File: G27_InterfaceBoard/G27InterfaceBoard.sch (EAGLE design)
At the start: 32 parts, among them IC1 LMV321M5, IC2 74HC126D, J1 Pedal, J2 Shifter, U1 LMV324

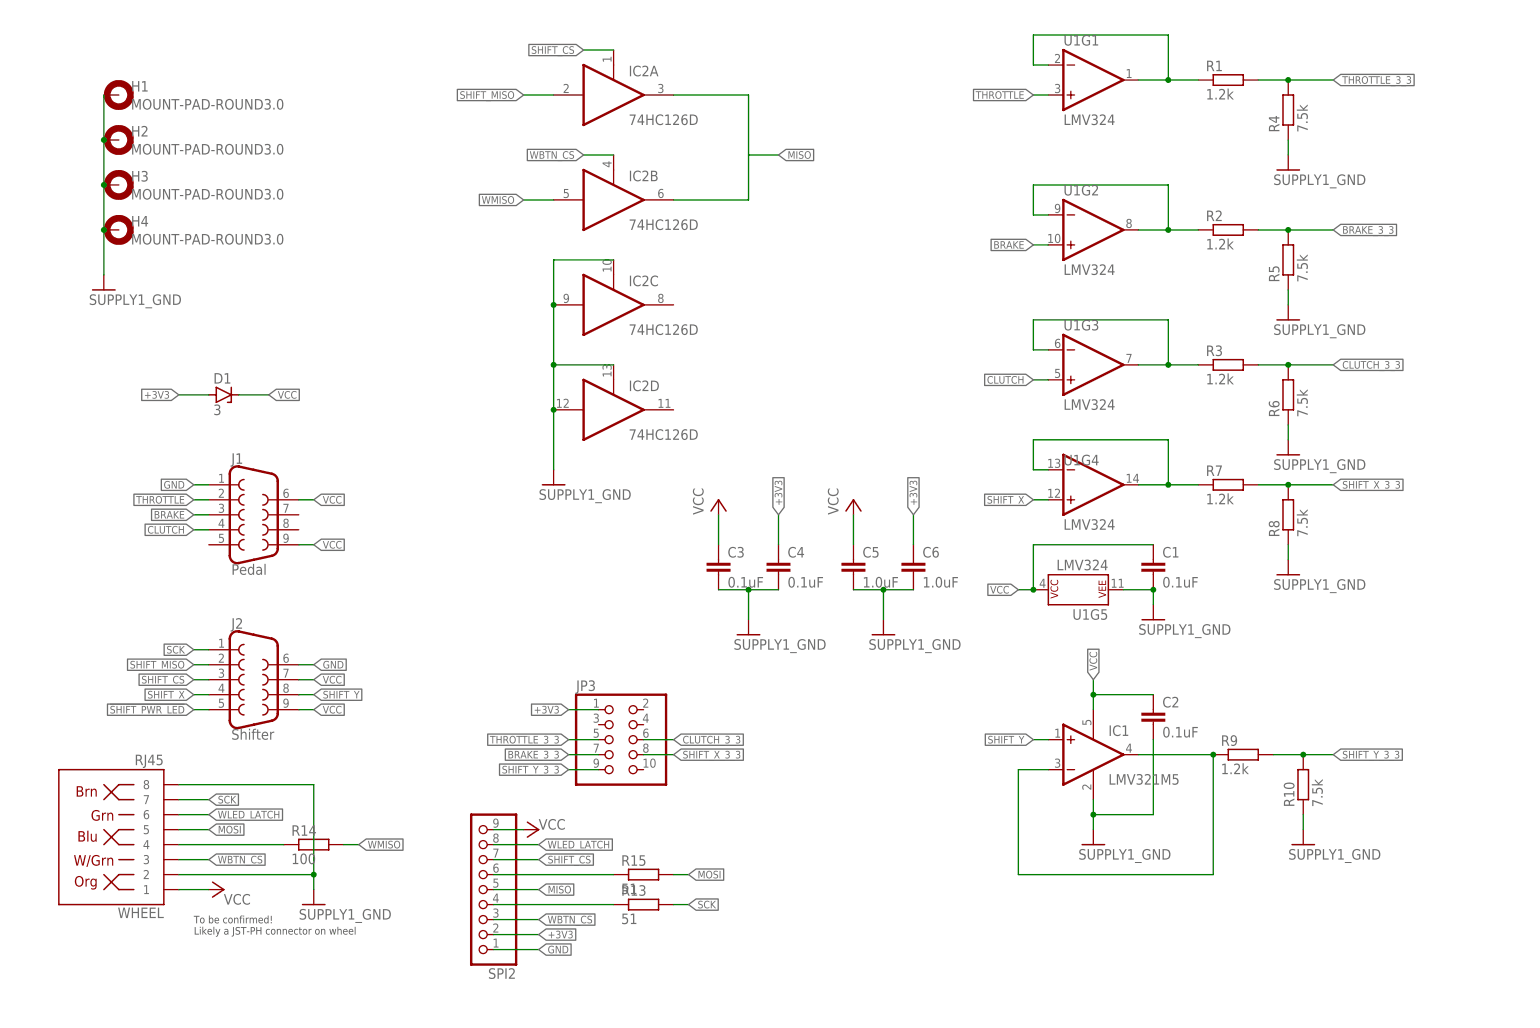
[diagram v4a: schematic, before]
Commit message: Closer on G27 Interface v1.1:
Use buffer to boost 3.3V signals from STM32 to 5V logic to buy
better noise margin.
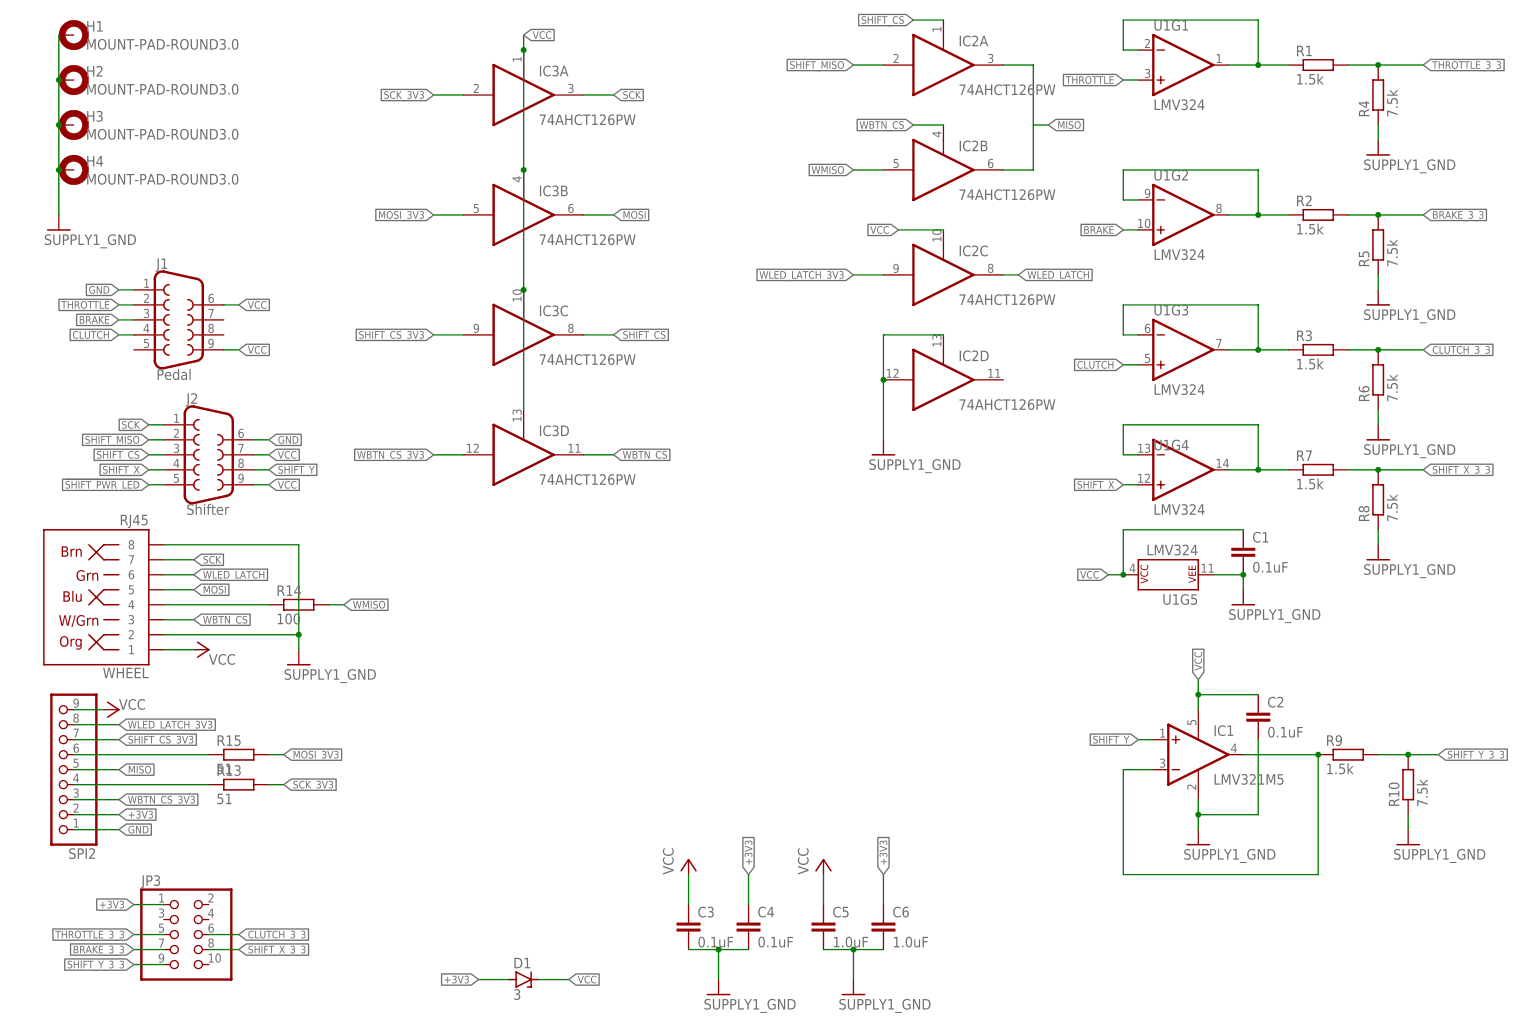
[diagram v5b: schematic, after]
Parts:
- added IC3: 74AHCT126PW, 74xx-eu:74AHCT126PW
- IC2: value 74HC126D -> 74AHCT126PW; device 74xx-eu:74HC126D -> 74xx-eu:74AHCT126PW
- R1, R2, R3, R7, R9: value 1.2k -> 1.5k
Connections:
- new net MOSI_3V3: IC3B.I, R15.2
- new net SCK_3V3: IC3A.I, R13.2
- new net SHIFT_CS_3V3: IC3C.I, SPI2.7
- new net WBTN_CS_3V3: IC3D.I, SPI2.3
- new net WLED_LATCH_3V3: IC2C.I, SPI2.8
- net GND: no longer IC2C.I, IC2C.OE
- net MOSI: now also IC3B.O; no longer R15.2
- net SCK: now also IC3A.O; no longer R13.2
- net SHIFT_CS: now also IC3C.O; no longer SPI2.7
- net VCC: now also IC2C.OE, IC3A.OE, IC3B.OE, IC3C.OE, IC3D.OE
- net WBTN_CS: now also IC3D.O; no longer SPI2.3
- net WLED_LATCH: now also IC2C.O; no longer SPI2.8
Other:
- note removed: "To be confirmed! Likely a JST-PH connector on wheel"
- moved on the sheet: C1, C2, C3, C4, C5, C6, D1, H1, H2, H3, H4, IC1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

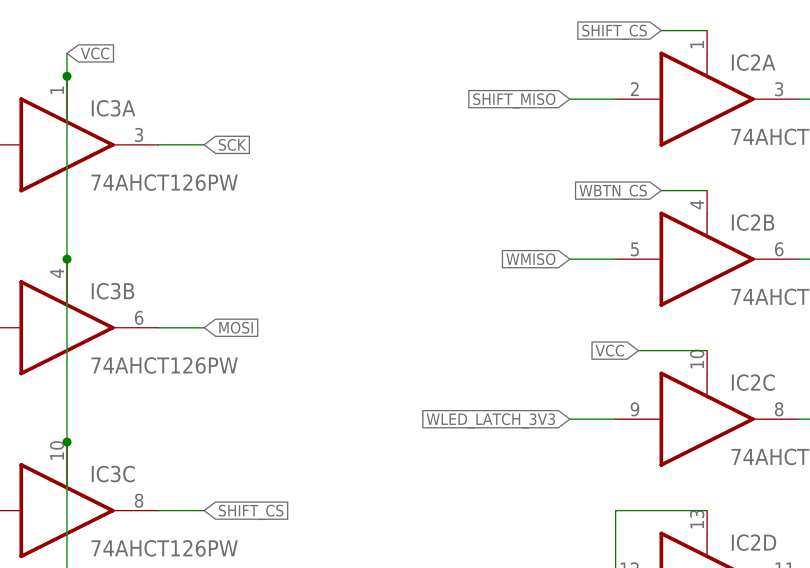
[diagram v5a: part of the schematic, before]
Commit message: Add additional filter caps.
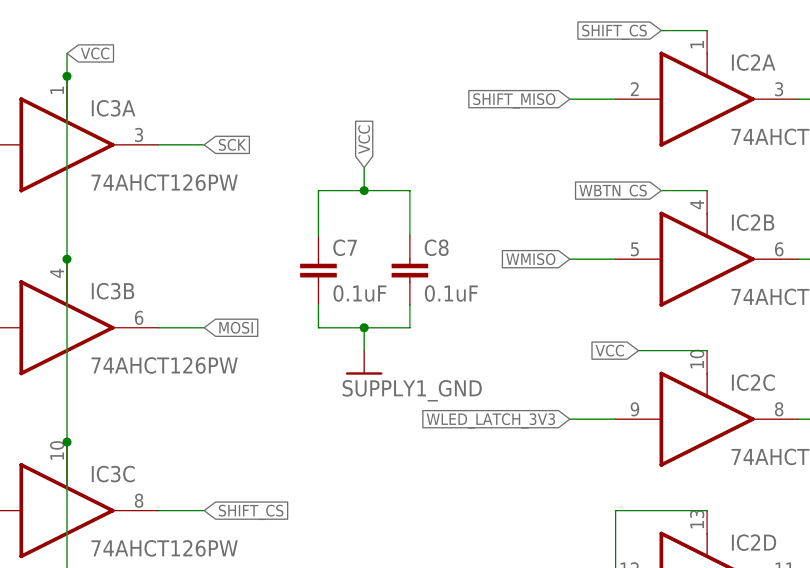
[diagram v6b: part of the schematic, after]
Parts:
- added C7, C8: 0.1uF, resistor:C-EUC0603
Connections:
- net GND: now also C7.2, C8.2
- net VCC: now also C7.1, C8.1
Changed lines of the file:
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@@
 <part name="R15" library="resistor" library_urn="urn:adsk.eagle:library:348" deviceset="R-EU_" device="R0603" package3d_urn="urn:adsk.eagle:package:23555/3" value="51"/>
 <part name="IC3" library="74xx-eu" deviceset="74*126" device="PW" package3d_urn="urn:adsk.eagle:package:2019/3" technology="AHCT"/>
+<part name="C7" library="resistor" library_urn="urn:adsk.eagle:library:348" deviceset="C-EU" device="C0603" package3d_urn="urn:adsk.eagle:package:23616/2" value="0.1uF"/>
+<part name="C8" library="resistor" library_urn="urn:adsk.eagle:library:348" deviceset="C-EU" device="C0603" package3d_urn="urn:adsk.eagle:package:23616/2" value="0.1uF"/>
+<part name="GND13" library="stm_board_f407" deviceset="SUPPLY1_GND" device=""/>
 </parts>
 <sheets>
@@
 <attribute name="NAME" x="88.9" y="102.235" size="1.778" layer="95"/>
 <attribute name="VALUE" x="88.9" y="93.98" size="1.778" layer="96"/>
+</instance>
+<instance part="C7" gate="G$1" x="114.3" y="147.32" smashed="yes">
+<attribute name="NAME" x="115.824" y="147.701" size="1.778" layer="95"/>
+<attribute name="VALUE" x="115.824" y="142.621" size="1.778" layer="96"/>
+</instance>
+<instance part="C8" gate="G$1" x="124.46" y="147.32" smashed="yes">
+<attribute name="NAME" x="125.984" y="147.701" size="1.778" layer="95"/>
+<attribute name="VALUE" x="125.984" y="142.621" size="1.778" layer="96"/>
+</instance>
+<instance part="GND13" gate="1" x="119.38" y="134.62" smashed="yes">
+<attribute name="VALUE" x="116.84" y="132.08" size="1.778" layer="96"/>
 </instance>
 </instances>
@@
 <label x="17.78" y="35.56" size="1.27" layer="95" xref="yes"/>
 </segment>
+<segment>
+<pinref part="C7" gate="G$1" pin="2"/>
+<wire x1="114.3" y1="142.24" x2="114.3" y2="139.7" width="0.1524" layer="91"/>
+<pinref part="C8" gate="G$1" pin="2"/>
+<wire x1="114.3" y1="139.7" x2="119.38" y2="139.7" width="0.1524" layer="91"/>
+<wire x1="119.38" y1="139.7" x2="124.46" y2="139.7" width="0.1524" layer="91"/>
+<wire x1="124.46" y1="139.7" x2="124.46" y2="142.24" width="0.1524" layer="91"/>
+<junction x="119.38" y="139.7"/>
+<pinref part="GND13" gate="1" pin="GND"/>
+<wire x1="119.38" y1="137.16" x2="119.38" y2="139.7" width="0.1524" layer="91"/>
+</segment>
 </net>
 <net name="SCK" class="0">
@@
 <junction x="86.36" y="127"/>
 </segment>
-</net>
+<segment>
+<pinref part="C7" gate="G$1" pin="1"/>
+<wire x1="114.3" y1="149.86" x2="114.3" y2="154.94" width="0.1524" layer="91"/>
+<pinref part="C8" gate="G$1" pin="1"/>
+<wire x1="114.3" y1="154.94" x2="119.38" y2="154.94" width="0.1524" layer="91"/>
+<wire x1="119.38" y1="154.94" x2="124.46" y2="154.94" width="0.1524" layer="91"/>
+<wire x1="124.46" y1="154.94" x2="124.46" y2="149.86" width="0.1524" layer="91"/>
+<junction x="119.38" y="154.94"/>
+<wire x1="119.38" y1="154.94" x2="119.38" y2="157.48" width="0.1524" layer="91"/>
+<label x="119.38" y="157.48" size="1.27" layer="95" rot="R90" xref="yes"/>
+</segment>
+</net>

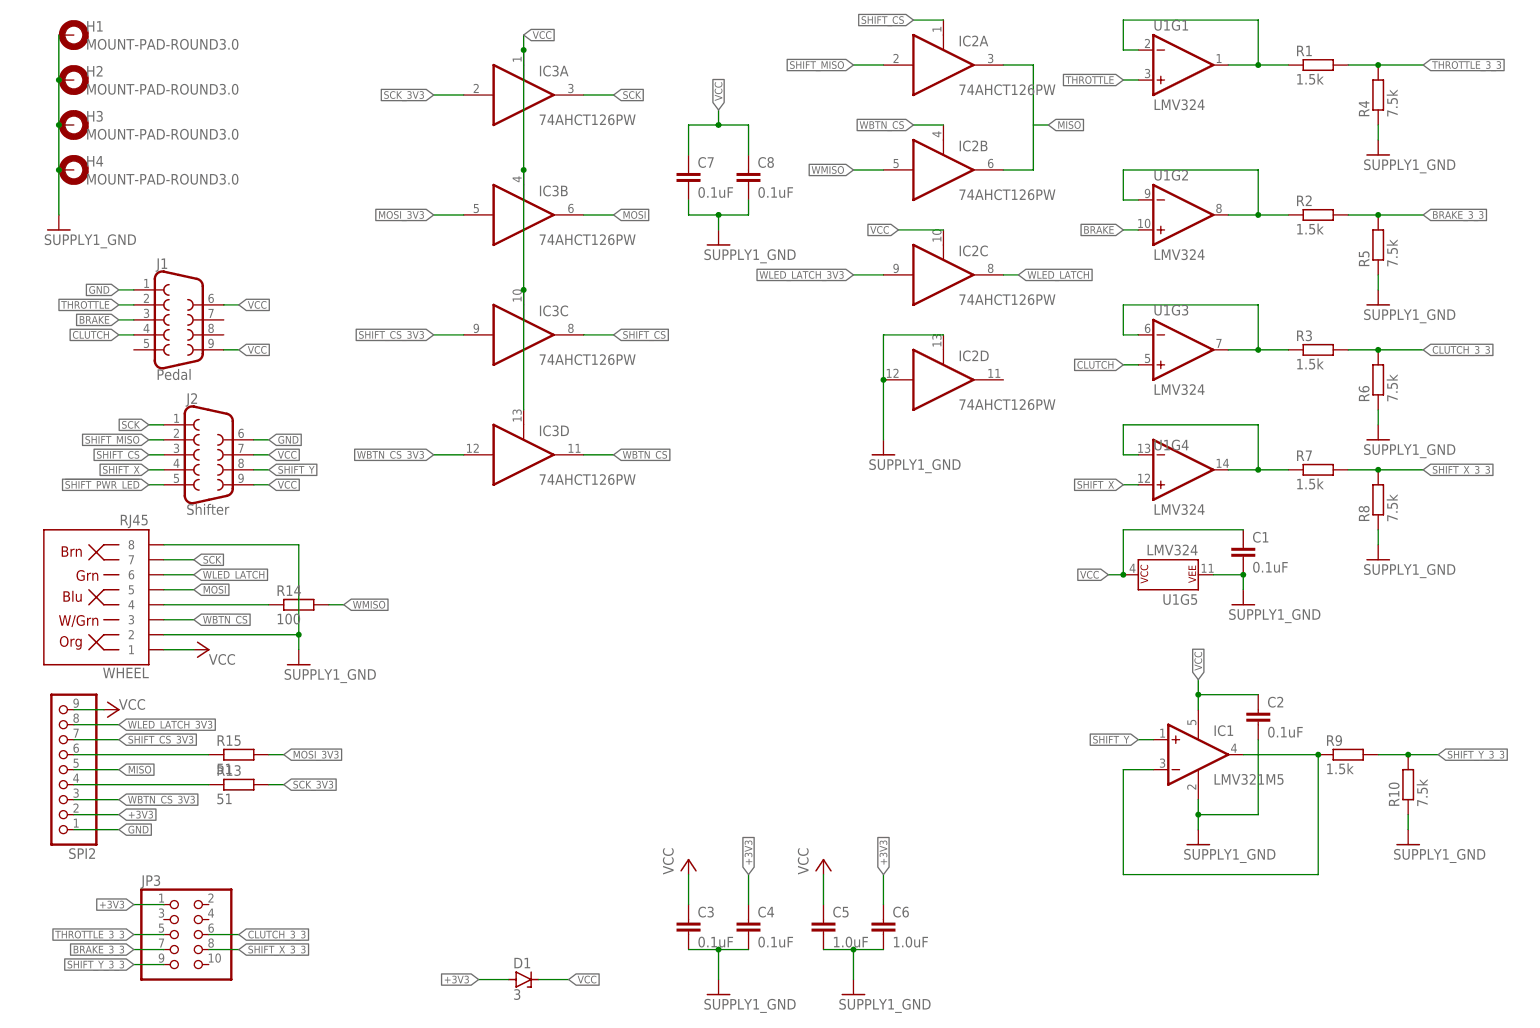
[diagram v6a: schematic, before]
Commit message: Add voltage clamps to signals that could go above 3.3V.
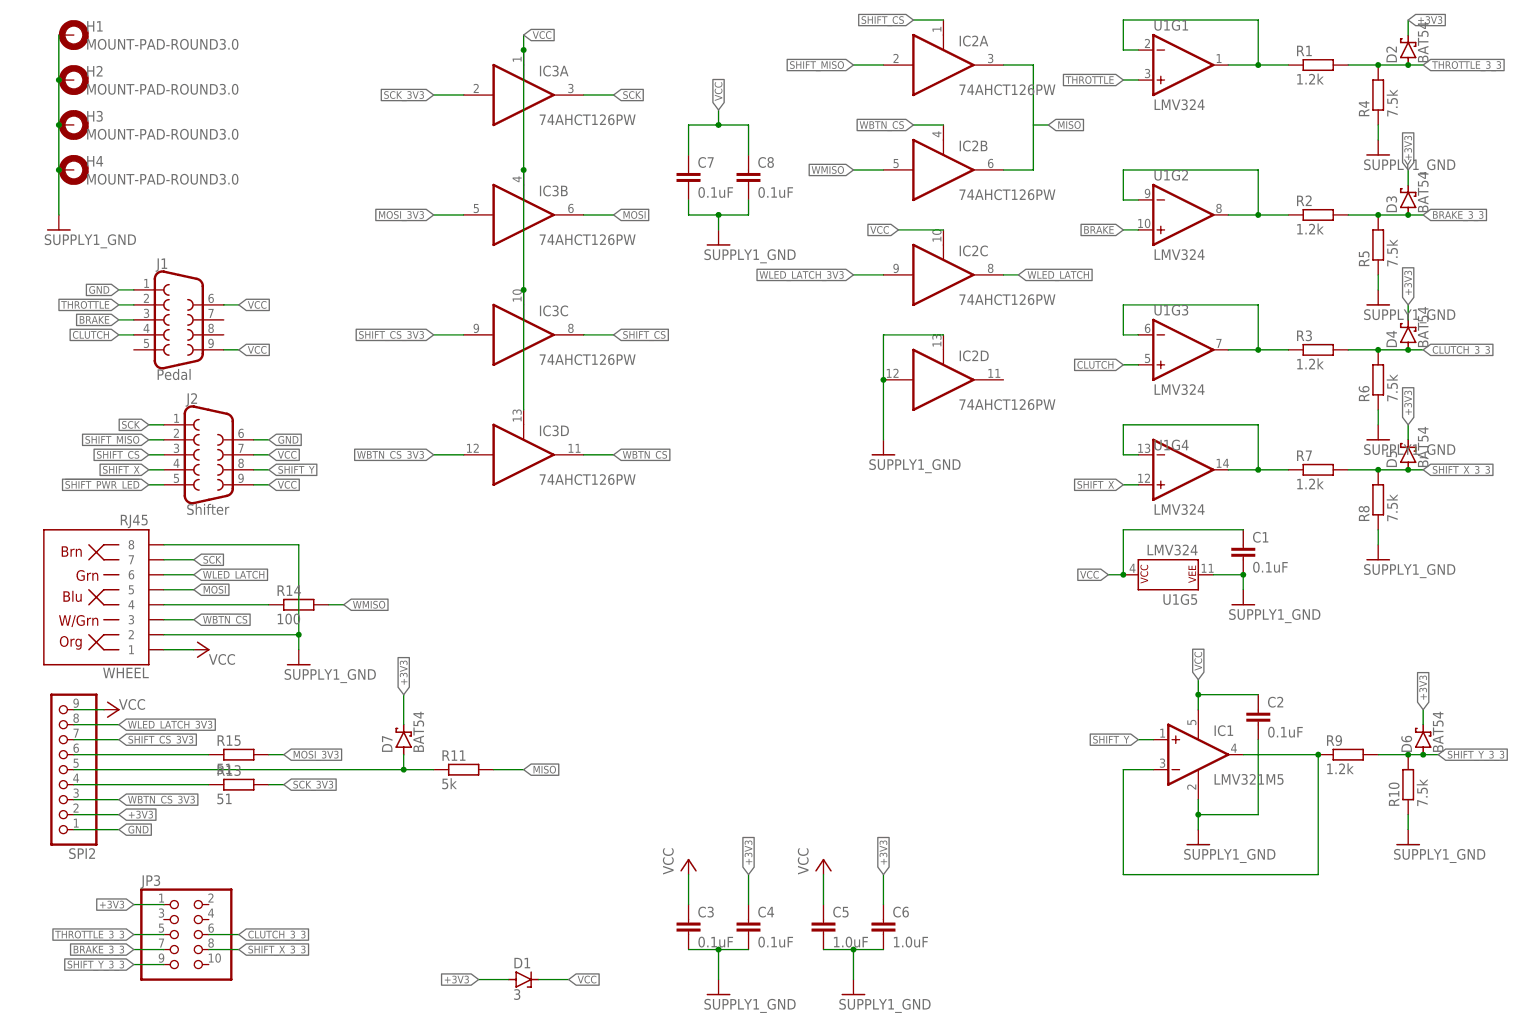
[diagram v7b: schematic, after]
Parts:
- added D2, D3, D4, D5, D6, D7: BAT54, diode:BAT54
- added R11: 5k, resistor:R-EU_R0603
- R1, R2, R3, R7, R9: value 1.5k -> 1.2k
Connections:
- new net N$4: D7.A, R11.1, SPI2.5
- net +3V3: now also D2.C, D3.C, D4.C, D5.C, D6.C, D7.C
- net BRAKE_3_3: now also D3.A
- net CLUTCH_3_3: now also D4.A
- net MISO: now also R11.2; no longer SPI2.5
- net SHIFT_X_3_3: now also D5.A
- net SHIFT_Y_3_3: now also D6.A
- net THROTTLE_3_3: now also D2.A

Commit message: Add better 5V, 3.3V, and GND connections.
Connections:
- net +3V3: now also JP3.2
- net GND: now also JP3.3, JP3.4
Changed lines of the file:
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@@
 <wire x1="119.38" y1="137.16" x2="119.38" y2="139.7" width="0.1524" layer="91"/>
+</segment>
+<segment>
+<pinref part="JP3" gate="A" pin="4"/>
+<wire x1="33.02" y1="20.32" x2="38.1" y2="20.32" width="0.1524" layer="91"/>
+<label x="38.1" y="20.32" size="1.27" layer="95" xref="yes"/>
+</segment>
+<segment>
+<pinref part="JP3" gate="A" pin="3"/>
+<wire x1="25.4" y1="20.32" x2="20.32" y2="20.32" width="0.1524" layer="91"/>
+<label x="20.32" y="20.32" size="1.27" layer="95" rot="R180" xref="yes"/>
 </segment>
 </net>
@@
 <label x="66.04" y="58.42" size="1.27" layer="95" rot="R90" xref="yes"/>
 </segment>
-</net>
+<segment>
+<pinref part="JP3" gate="A" pin="2"/>
+<wire x1="33.02" y1="22.86" x2="38.1" y2="22.86" width="0.1524" layer="91"/>
+<label x="38.1" y="22.86" size="1.27" layer="95" xref="yes"/>
+</segment>
+</net>
